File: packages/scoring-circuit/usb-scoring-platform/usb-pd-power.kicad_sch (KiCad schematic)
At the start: 34 parts, among them J12 PD service: GND SDA SCL, Q4 DMN2056U-7, Q5 DMN2056U-7, U19 LMR36510ADDAR, U20 TPS259470LRPWR, U5 STUSB4500QTR, U6 REC30K-2405SZ

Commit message: fix(scoring-circuit): select service headers and correct drill sizes
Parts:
- J12: footprint Connector_PinHeader_2.54mm:PinHeader_1x03_P2.54mm_Vertical -> ScoringPlatform:Samtec_HTSW-103-07-L-S; MPN (none) -> HTSW-103-07-L-S; Manufacturer (none) -> Samtec
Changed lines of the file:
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@@
 (wire (pts (xy 144.78 87.63) (xy 139.7 87.63)) (stroke (width 0) (type default)))
 (global_label "PD_SCL" (shape bidirectional) (at 139.7 87.63 180) (effects (font (size .9 .9)) (justify right)) (property "Intersheetrefs" "" (at 139.7 87.63 180) (effects (font (size 1 1)) (hide yes))))
-(symbol (lib_id "Connector_Generic:Conn_01x03") (at 149.86 85.09 0) (unit 1) (in_bom yes) (on_board yes) (dnp no) (property "Reference" "J12" (at 149.86 69.85 0) (effects (font (size 1.2 1.2)))) (property "Value" "PD service: GND SDA SCL" (at 149.86 72.39 0) (effects (font (size 1.1 1.1)))) (property "Footprint" "Connector_PinHeader_2.54mm:PinHeader_1x03_P2.54mm_Vertical" (at 149.86 85.09 0) (effects (font (size 1 1)) (hide yes))) (property "Datasheet" "" (at 149.86 85.09 0) (effects (font (size 1 1)) (hide yes))) (instances (project "usb-scoring-platform" (path "/20cc8167-128c-446a-a106-f942323e143f/972b77fe-bd38-49a7-88fc-3c741d64cdb1" (reference "J12") (unit 1)))) (pin "1") (pin "2") (pin "3"))
+(symbol (lib_id "Connector_Generic:Conn_01x03") (at 149.86 85.09 0) (unit 1) (in_bom yes) (on_board yes) (dnp no) (property "Reference" "J12" (at 149.86 69.85 0) (effects (font (size 1.2 1.2)))) (property "Value" "PD service: GND SDA SCL" (at 149.86 72.39 0) (effects (font (size 1.1 1.1)))) (property "Footprint" "ScoringPlatform:Samtec_HTSW-103-07-L-S" (at 149.86 85.09 0) (effects (font (size 1 1)) (hide yes))) (property "Datasheet" "https://suddendocs.samtec.com/prints/htsw-xxx-xx-xxx-x-xx-xx-xx-mkt.pdf" (at 149.86 85.09 0) (effects (font (size 1 1)) (hide yes))) (instances (project "usb-scoring-platform" (path "/20cc8167-128c-446a-a106-f942323e143f/972b77fe-bd38-49a7-88fc-3c741d64cdb1" (reference "J12") (unit 1)))) (pin "1") (pin "2") (pin "3") (property "Manufacturer" "Samtec" (at 0 0 0) (effects (font (size 1 1)) (hide yes))) (property "MPN" "HTSW-103-07-L-S" (at 0 0 0) (effects (font (size 1 1)) (hide yes))))
 (wire (pts (xy 299.72 95.25) (xy 299.72 100.33)) (stroke (width 0) (type default)))
 (global_label "USB_GND" (shape bidirectional) (at 299.72 100.33 0) (effects (font (size .9 .9)) (justify left)) (property "Intersheetrefs" "" (at 299.72 100.33 0) (effects (font (size 1 1)) (hide yes))))

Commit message: chore(scoring-circuit): complete assembly BOM ordering fields
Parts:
- U19: MPN (none) -> LMR36510ADDAR; Manufacturer (none) -> Texas Instruments
- U20: MPN (none) -> TPS259470LRPWR; Manufacturer (none) -> Texas Instruments
- U5: MPN (none) -> STUSB4500QTR; Manufacturer (none) -> STMicroelectronics
- U6: MPN (none) -> REC30K-2405SZ; Manufacturer (none) -> RECOM
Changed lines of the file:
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@@
 (wire (pts (xy 87.63 62.23) (xy 87.63 57.15)) (stroke (width 0) (type default)))
 (global_label "USB_VBUS" (shape bidirectional) (at 87.63 57.15 90) (effects (font (size .9 .9)) (justify left)) (property "Intersheetrefs" "" (at 87.63 57.15 0) (effects (font (size 1 1)) (hide yes))))
-(symbol (lib_id "Interface_USB:STUSB4500QTR") (at 90.17 85.09 0) (unit 1) (in_bom yes) (on_board yes) (dnp no) (property "Reference" "U5" (at 137.16 53.34 0) (effects (font (size 1.2 1.2)))) (property "Value" "STUSB4500QTR" (at 137.16 55.88 0) (effects (font (size 1.1 1.1)))) (property "Footprint" "ScoringPlatform:STUSB4500QTR" (at 90.17 85.09 0) (effects (font (size 1 1)) (hide yes))) (property "Datasheet" "https://www.st.com/resource/en/datasheet/stusb4500.pdf" (at 90.17 85.09 0) (effects (font (size 1 1)) (hide yes))) (instances (project "usb-scoring-platform" (path "/20cc8167-128c-446a-a106-f942323e143f/972b77fe-bd38-49a7-88fc-3c741d64cdb1" (reference "U5") (unit 1)))) (pin "1") (pin "2") (pin "3") (pin "4") (pin "5") (pin "6") (pin "7") (pin "8") (pin "9") (pin "10") (pin "11") (pin "12") (pin "13") (pin "14") (pin "15") (pin "16") (pin "17") (pin "18") (pin "19") (pin "20") (pin "21") (pin "22") (pin "23") (pin "24") (pin "25"))
+(symbol (lib_id "Interface_USB:STUSB4500QTR") (at 90.17 85.09 0) (unit 1) (in_bom yes) (on_board yes) (dnp no) (property "Reference" "U5" (at 137.16 53.34 0) (effects (font (size 1.2 1.2)))) (property "Value" "STUSB4500QTR" (at 137.16 55.88 0) (effects (font (size 1.1 1.1)))) (property "Footprint" "ScoringPlatform:STUSB4500QTR" (at 90.17 85.09 0) (effects (font (size 1 1)) (hide yes))) (property "Datasheet" "https://www.st.com/resource/en/datasheet/stusb4500.pdf" (at 90.17 85.09 0) (effects (font (size 1 1)) (hide yes))) (instances (project "usb-scoring-platform" (path "/20cc8167-128c-446a-a106-f942323e143f/972b77fe-bd38-49a7-88fc-3c741d64cdb1" (reference "U5") (unit 1)))) (pin "1") (pin "2") (pin "3") (pin "4") (pin "5") (pin "6") (pin "7") (pin "8") (pin "9") (pin "10") (pin "11") (pin "12") (pin "13") (pin "14") (pin "15") (pin "16") (pin "17") (pin "18") (pin "19") (pin "20") (pin "21") (pin "22") (pin "23") (pin "24") (pin "25") (property "Manufacturer" "STMicroelectronics" (at 0 0 0) (effects (font (size 1 1)) (hide yes))) (property "MPN" "STUSB4500QTR" (at 0 0 0) (effects (font (size 1 1)) (hide yes))))
 (wire (pts (xy 39.37 146.05) (xy 39.37 140.97)) (stroke (width 0) (type default)))
 (global_label "USB_VBUS" (shape bidirectional) (at 39.37 140.97 0) (effects (font (size .9 .9)) (justify left)) (property "Intersheetrefs" "" (at 39.37 140.97 0) (effects (font (size 1 1)) (hide yes))))
@@
 (wire (pts (xy 302.26 95.25) (xy 302.26 100.33)) (stroke (width 0) (type default)))
 (global_label "USB_GND" (shape bidirectional) (at 302.26 100.33 0) (effects (font (size .9 .9)) (justify left)) (property "Intersheetrefs" "" (at 302.26 100.33 0) (effects (font (size 1 1)) (hide yes))))
-(symbol (lib_id "Regulator_Switching:LMR36510ADDA") (at 299.72 85.09 0) (unit 1) (in_bom yes) (on_board yes) (dnp no) (property "Reference" "U19" (at 299.72 67.31 0) (effects (font (size 1.2 1.2)))) (property "Value" "LMR36510ADDAR" (at 299.72 69.85000000000001 0) (effects (font (size 1.1 1.1)))) (property "Footprint" "Package_SO:Texas_HTSOP-8-1EP_3.9x4.9mm_P1.27mm_EP2.95x4.9mm_Mask2.4x3.1mm_ThermalVias" (at 299.72 85.09 0) (effects (font (size 1 1)) (hide yes))) (property "Datasheet" "http://www.ti.com/lit/ds/symlink/lmr36510.pdf" (at 299.72 85.09 0) (effects (font (size 1 1)) (hide yes))) (instances (project "usb-scoring-platform" (path "/20cc8167-128c-446a-a106-f942323e143f/972b77fe-bd38-49a7-88fc-3c741d64cdb1" (reference "U19") (unit 1)))) (pin "1") (pin "2") (pin "3") (pin "4") (pin "5") (pin "6") (pin "7") (pin "8") (pin "9"))
+(symbol (lib_id "Regulator_Switching:LMR36510ADDA") (at 299.72 85.09 0) (unit 1) (in_bom yes) (on_board yes) (dnp no) (property "Reference" "U19" (at 299.72 67.31 0) (effects (font (size 1.2 1.2)))) (property "Value" "LMR36510ADDAR" (at 299.72 69.85000000000001 0) (effects (font (size 1.1 1.1)))) (property "Footprint" "Package_SO:Texas_HTSOP-8-1EP_3.9x4.9mm_P1.27mm_EP2.95x4.9mm_Mask2.4x3.1mm_ThermalVias" (at 299.72 85.09 0) (effects (font (size 1 1)) (hide yes))) (property "Datasheet" "http://www.ti.com/lit/ds/symlink/lmr36510.pdf" (at 299.72 85.09 0) (effects (font (size 1 1)) (hide yes))) (instances (project "usb-scoring-platform" (path "/20cc8167-128c-446a-a106-f942323e143f/972b77fe-bd38-49a7-88fc-3c741d64cdb1" (reference "U19") (unit 1)))) (pin "1") (pin "2") (pin "3") (pin "4") (pin "5") (pin "6") (pin "7") (pin "8") (pin "9") (property "Manufacturer" "Texas Instruments" (at 0 0 0) (effects (font (size 1 1)) (hide yes))) (property "MPN" "LMR36510ADDAR" (at 0 0 0) (effects (font (size 1 1)) (hide yes))))
 (wire (pts (xy 364.49 81.28) (xy 364.49 76.2)) (stroke (width 0) (type default)))
 (global_label "USB_BUCK_SW" (shape bidirectional) (at 364.49 76.2 0) (effects (font (size .9 .9)) (justify left)) (property "Intersheetrefs" "" (at 364.49 76.2 0) (effects (font (size 1 1)) (hide yes))))
@@
 (wire (pts (xy 317.5 245.11) (xy 322.58 245.11)) (stroke (width 0) (type default)))
 (global_label "USB_GND" (shape bidirectional) (at 322.58 245.11 0) (effects (font (size .9 .9)) (justify left)) (property "Intersheetrefs" "" (at 322.58 245.11 0) (effects (font (size 1 1)) (hide yes))))
-(symbol (lib_id "ScoringPlatform:TPS259470LRPWR") (at 299.72 240.03 0) (unit 1) (in_bom yes) (on_board yes) (dnp no) (property "Reference" "U20" (at 299.72 222.25 0) (effects (font (size 1.2 1.2)))) (property "Value" "TPS259470LRPWR" (at 299.72 224.79 0) (effects (font (size 1.1 1.1)))) (property "Footprint" "ScoringPlatform:TPS259470LRPWR" (at 299.72 240.03 0) (effects (font (size 1 1)) (hide yes))) (property "Datasheet" "https://www.ti.com/lit/ds/symlink/tps25947.pdf" (at 299.72 240.03 0) (effects (font (size 1 1)) (hide yes))) (instances (project "usb-scoring-platform" (path "/20cc8167-128c-446a-a106-f942323e143f/972b77fe-bd38-49a7-88fc-3c741d64cdb1" (reference "U20") (unit 1)))) (pin "5") (pin "1") (pin "2") (pin "3") (pin "10") (pin "6") (pin "4") (pin "7") (pin "9") (pin "8"))
+(symbol (lib_id "ScoringPlatform:TPS259470LRPWR") (at 299.72 240.03 0) (unit 1) (in_bom yes) (on_board yes) (dnp no) (property "Reference" "U20" (at 299.72 222.25 0) (effects (font (size 1.2 1.2)))) (property "Value" "TPS259470LRPWR" (at 299.72 224.79 0) (effects (font (size 1.1 1.1)))) (property "Footprint" "ScoringPlatform:TPS259470LRPWR" (at 299.72 240.03 0) (effects (font (size 1 1)) (hide yes))) (property "Datasheet" "https://www.ti.com/lit/ds/symlink/tps25947.pdf" (at 299.72 240.03 0) (effects (font (size 1 1)) (hide yes))) (instances (project "usb-scoring-platform" (path "/20cc8167-128c-446a-a106-f942323e143f/972b77fe-bd38-49a7-88fc-3c741d64cdb1" (reference "U20") (unit 1)))) (pin "5") (pin "1") (pin "2") (pin "3") (pin "10") (pin "6") (pin "4") (pin "7") (pin "9") (pin "8") (property "Manufacturer" "Texas Instruments" (at 0 0 0) (effects (font (size 1 1)) (hide yes))) (property "MPN" "TPS259470LRPWR" (at 0 0 0) (effects (font (size 1 1)) (hide yes))))
 (wire (pts (xy 447.04 237.49) (xy 441.96 237.49)) (stroke (width 0) (type default)))
 (global_label "PD_ISO_INPUT" (shape bidirectional) (at 441.96 237.49 180) (effects (font (size .9 .9)) (justify right)) (property "Intersheetrefs" "" (at 441.96 237.49 180) (effects (font (size 1 1)) (hide yes))))
@@
 (global_label "GND" (shape bidirectional) (at 487.68 240.03 0) (effects (font (size .9 .9)) (justify left)) (property "Intersheetrefs" "" (at 487.68 240.03 0) (effects (font (size 1 1)) (hide yes))))
 (no_connect (at 482.6 242.57))
-(symbol (lib_id "ScoringPlatform:REC30K-2405SZ") (at 464.82 240.03 0) (unit 1) (in_bom yes) (on_board yes) (dnp no) (property "Reference" "U6" (at 464.82 224.79000000000002 0) (effects (font (size 1.2 1.2)))) (property "Value" "REC30K-2405SZ" (at 464.82 227.33 0) (effects (font (size 1.1 1.1)))) (property "Footprint" "ScoringPlatform:REC30K-2405SZ" (at 464.82 240.03 0) (effects (font (size 1 1)) (hide yes))) (property "Datasheet" "https://g.recomcdn.com/media/Datasheet/pdf/REC30K(-Z).pdf" (at 464.82 240.03 0) (effects (font (size 1 1)) (hide yes))) (instances (project "usb-scoring-platform" (path "/20cc8167-128c-446a-a106-f942323e143f/972b77fe-bd38-49a7-88fc-3c741d64cdb1" (reference "U6") (unit 1)))) (pin "1") (pin "2") (pin "3") (pin "6") (pin "4") (pin "5"))
+(symbol (lib_id "ScoringPlatform:REC30K-2405SZ") (at 464.82 240.03 0) (unit 1) (in_bom yes) (on_board yes) (dnp no) (property "Reference" "U6" (at 464.82 224.79000000000002 0) (effects (font (size 1.2 1.2)))) (property "Value" "REC30K-2405SZ" (at 464.82 227.33 0) (effects (font (size 1.1 1.1)))) (property "Footprint" "ScoringPlatform:REC30K-2405SZ" (at 464.82 240.03 0) (effects (font (size 1 1)) (hide yes))) (property "Datasheet" "https://g.recomcdn.com/media/Datasheet/pdf/REC30K(-Z).pdf" (at 464.82 240.03 0) (effects (font (size 1 1)) (hide yes))) (instances (project "usb-scoring-platform" (path "/20cc8167-128c-446a-a106-f942323e143f/972b77fe-bd38-49a7-88fc-3c741d64cdb1" (reference "U6") (unit 1)))) (pin "1") (pin "2") (pin "3") (pin "6") (pin "4") (pin "5") (property "Manufacturer" "RECOM" (at 0 0 0) (effects (font (size 1 1)) (hide yes))) (property "MPN" "REC30K-2405SZ" (at 0 0 0) (effects (font (size 1 1)) (hide yes))))
 (wire (pts (xy 59.69 245.11) (xy 54.61 245.11)) (stroke (width 0) (type default)))
 (global_label "PD_20V_OK_N" (shape bidirectional) (at 54.61 245.11 180) (effects (font (size .9 .9)) (justify right)) (property "Intersheetrefs" "" (at 54.61 245.11 180) (effects (font (size 1 1)) (hide yes))))

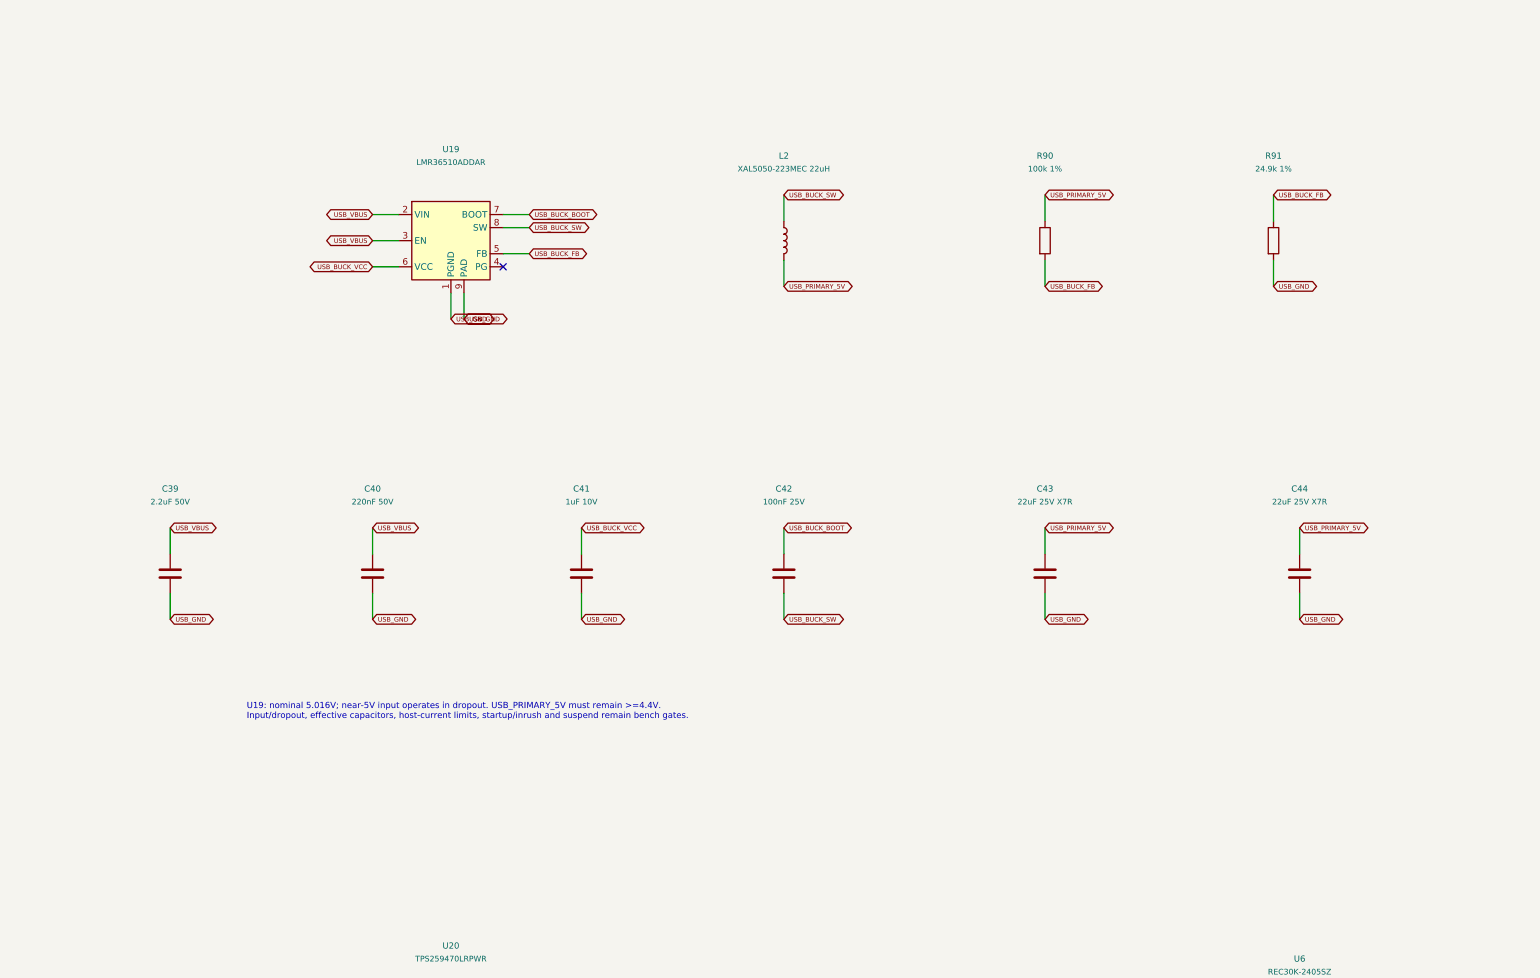
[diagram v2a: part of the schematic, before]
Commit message: fix(scoring-circuit): regulate isolated USB supply across input range
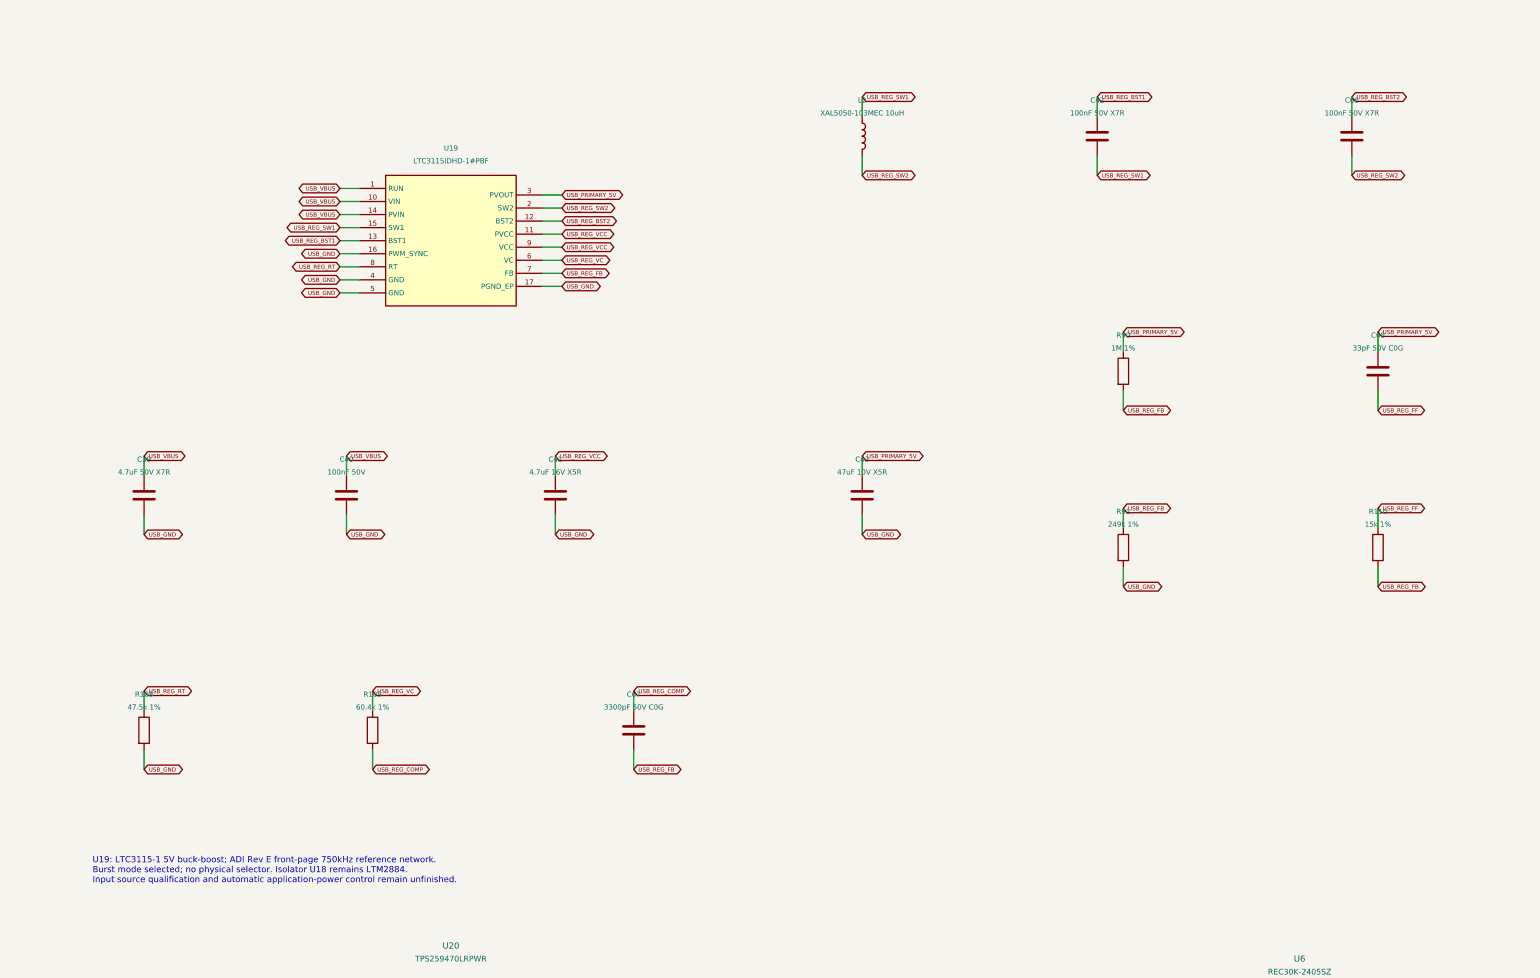
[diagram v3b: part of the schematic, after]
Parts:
- removed C44: 22uF 25V X7R, Capacitor_SMD:C_1210_3225Metric, symbol Device:C
- added C66: 100nF 50V X7R, Capacitor_SMD:C_0603_1608Metric, symbol Device:C
- added C67: 3300pF 50V C0G, Capacitor_SMD:C_0603_1608Metric, symbol Device:C
- added C68: 33pF 50V C0G, Capacitor_SMD:C_0603_1608Metric, symbol Device:C
- added R108: 47.5k 1%, Resistor_SMD:R_0603_1608Metric, symbol Device:R
- added R109: 60.4k 1%, Resistor_SMD:R_0603_1608Metric, symbol Device:R
- added R110: 15k 1%, Resistor_SMD:R_0603_1608Metric, symbol Device:R
- C39: value 2.2uF 50V -> 4.7uF 50V X7R; footprint Capacitor_SMD:C_1206_3216Metric -> Capacitor_SMD:C_1812_4532Metric; MPN C3216X7R1H225K160AB -> C4532X7R1H475K200KB
- C40: value 220nF 50V -> 100nF 50V; MPN C2012X7R1H224K125AA -> C2012X7R1H104K085AA
- C41: value 1uF 10V -> 4.7uF 16V X5R; footprint Capacitor_SMD:C_0603_1608Metric -> Capacitor_SMD:C_0805_2012Metric; MPN C1608X7R1H105K080AB -> C2012X5R1C475K125AC
- C42: value 100nF 25V -> 100nF 50V X7R
- C43: value 22uF 25V X7R -> 47uF 10V X5R; footprint Capacitor_SMD:C_1210_3225Metric -> Capacitor_SMD:C_1812_4532Metric; MPN GRM32ER71E226KE15L -> C4532X5R1A476M280KA; Manufacturer Murata -> TDK
- L2: value XAL5050-223MEC 22uH -> XAL5050-103MEC 10uH; MPN XAL5050-223MEC -> XAL5050-103MEC
- R90: value 100k 1% -> 1M 1%; MPN RC0603FR-07100KL -> RC0603FR-071ML
- R91: value 24.9k 1% -> 249k 1%; MPN RC0603FR-0724K9L -> RC0603FR-07249KL
- U19: value LMR36510ADDAR -> LTC3115IDHD-1#PBF; footprint Package_SO:Texas_HTSOP-8-1EP_3.9x4.9mm_P1.27mm_EP2.95x4.9mm_Mask2.4x3.1mm_ThermalVias -> Package_DFN_QFN:DFN-16-1EP_4x5mm_P0.5mm_EP2.44x4.34mm; symbol Regulator_Switching:LMR36510ADDA -> ScoringPlatform:LTC3115IDHD-1; MPN LMR36510ADDAR -> LTC3115IDHD-1#PBF; Manufacturer Texas Instruments -> Analog Devices
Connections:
- net USB_GND: now also U19.16 (PWM_SYNC), U19.17 (PGND_EP), U19.4 (GND), U19.5 (GND), R108.2; no longer U19.1 (PGND), U19.9 (PAD)
- net USB_PRIMARY_5V: now also U19.3 (PVOUT), C68.1; no longer L2.2
- net USB_VBUS: now also U19.1 (RUN), U19.10 (VIN), U19.14 (PVIN); no longer U19.2 (VIN), U19.3 (EN)
- net USB_BUCK_BOOT renamed USB_REG_BST1
- net USB_REG_BST1: now also U19.13 (BST1); no longer U19.7 (BOOT)
- net USB_BUCK_FB renamed USB_REG_FB
- net USB_REG_FB: now also U19.7 (FB), C67.2, R110.2; no longer U19.5 (FB)
- net USB_BUCK_SW renamed USB_REG_SW1
- net USB_REG_SW1: now also U19.15 (SW1); no longer U19.8 (SW)
- net USB_BUCK_VCC renamed USB_REG_VC
- net USB_REG_VC: now also R109.1; no longer C41.1
- new net USB_REG_BST2: C66.1, U19.12 (BST2)
- new net USB_REG_COMP: C67.1, R109.2
- new net USB_REG_FF: C68.2, R110.1
- new net USB_REG_RT: R108.1, U19.8 (RT)
- new net USB_REG_SW2: C66.2, L2.2, U19.2 (SW2)
- new net USB_REG_VCC: C41.1, U19.11 (PVCC), U19.9 (VCC)
- no-connect marks 12 -> 11
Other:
- note added: "U19: LTC3115-1 5V buck-boost; ADI Rev E front-page 750kHz reference network. Burst mode selected; no physical selector. Isolator U18 remains LTM2884. Input source qualification and automatic application-power control remain unfinished."
- note removed: "U19: nominal 5.016V; near-5V input operates in dropout. USB_PRIMARY_5V must remain >=4.4V. Input/dropout, effective capacitors, host-current limits, startup/inrush and suspend remain bench gates."
- moved on the sheet: C39, C40, C41, C42, C43, L2, R90, R91
